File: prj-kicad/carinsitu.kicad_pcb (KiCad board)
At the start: 2 copper layers, 0 parts

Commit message: = ADD: Draw board outline, add fix holes
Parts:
- added FIX1: CONN_1, carinsitu:FIX, F.Cu at (100.8, 101.0)
- added FIX2: CONN_1, carinsitu:FIX, F.Cu at (100.8, 109.0)
- added FIX3: CONN_1, carinsitu:FIX, F.Cu at (175.2, 105.0)
- added FIX4: CONN_1, carinsitu:FIX, F.Cu at (190.8, 101.0)
- added FIX5: CONN_1, carinsitu:FIX, F.Cu at (190.8, 109.0)
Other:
- board outline added: 131.5 x 50 mm

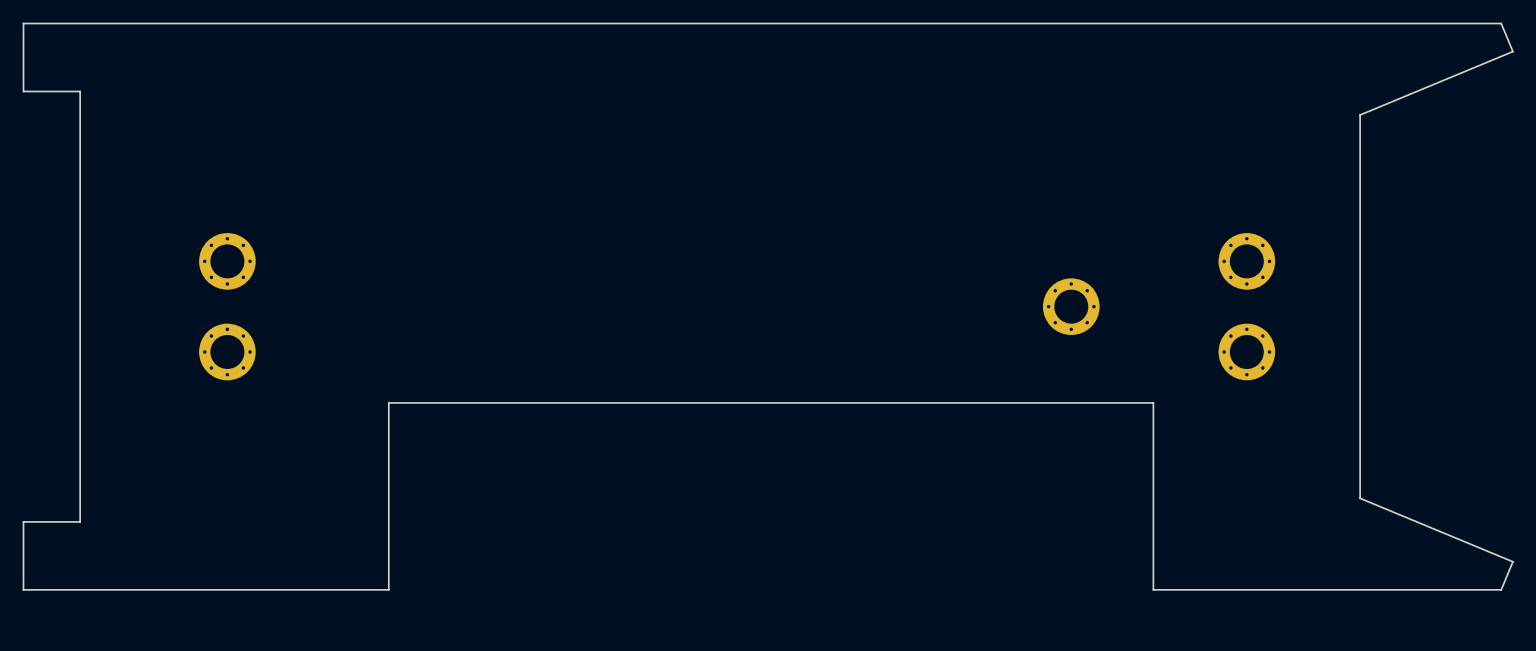
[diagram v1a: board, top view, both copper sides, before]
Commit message: = ADD: Place headlight LEDs, motor connector and ESC outline
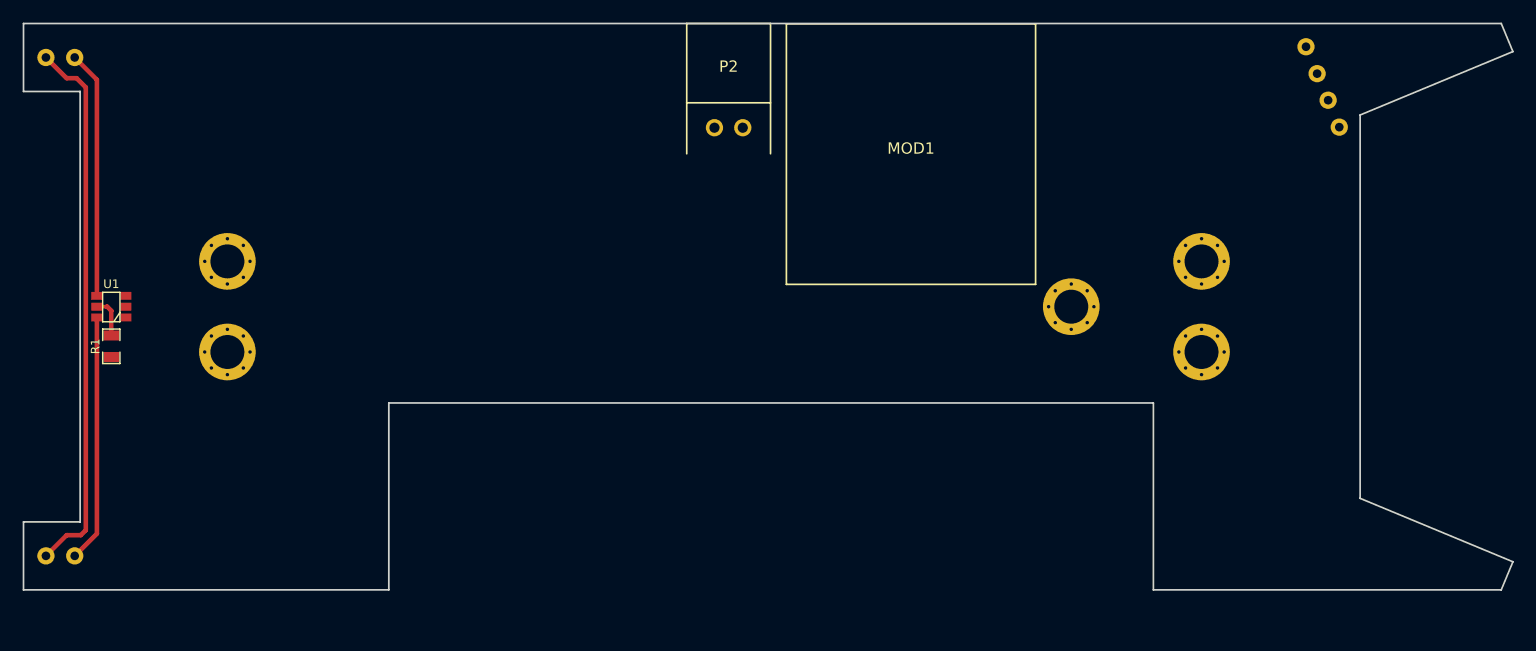
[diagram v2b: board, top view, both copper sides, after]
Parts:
- added D1: LED, carinsitu:LED, F.Cu at (86.0, 127.0)
- added D2: LED, carinsitu:LED, F.Cu at (86.0, 83.0)
- added MOD1: ESC, carinsitu:ESC, F.Cu at (161.1, 91.5)
- added P2: MOT, carinsitu:CONN_JST-XH-2, F.Cu at (145.0, 87.0)
- added R1: 10k, carinsitu:SMD0805, F.Cu at (90.5, 108.5)
- added REF**: LED-APA106, carinsitu:LED-APA106, F.Cu at (197.4, 85.6)
- added U1: MIC2860, carinsitu:SOT23-6, F.Cu at (90.5, 105.0)
- moved FIX4 4.00 mm to (186.8, 101.0)
- moved FIX5 4.00 mm to (186.8, 109.0)
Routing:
- net +5V: track 0.00 -> 48.2 mm
- net Net-(D2-Pad2): track 0.00 -> 21.9 mm
- net Net-(D1-Pad2): track 0.00 -> 21.9 mm
- net Net-(R1-Pad2): track 0.00 -> 3.61 mm
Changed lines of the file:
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@@
 (kicad_pcb (version 4) (host pcbnew 4.0.2+dfsg1-stable)
   (general
-    (links 44)
-    (no_connects 4)
+    (links 51)
+    (no_connects 7)
     (area 82.674999 79.924999 214.315001 130.075001)
     (thickness 1.6)
-    (drawings 23)
-    (tracks 0)
+    (drawings 25)
+    (tracks 15)
     (zones 0)
-    (modules 5)
-    (nets 2)
+    (modules 12)
+    (nets 9)
   )
   (page A4)
@@
   )
   (setup
-    (last_trace_width 0.25)
+    (last_trace_width 0.4064)
+    (user_trace_width 0.2032)
+    (user_trace_width 0.3048)
+    (user_trace_width 0.4064)
     (trace_clearance 0.2)
     (zone_clearance 0.508)
@@
   (net 0 "")
   (net 1 GND)
+  (net 2 "Net-(MOD1-Pad2)")
+  (net 3 "Net-(MOD1-Pad3)")
+  (net 4 +5V)
+  (net 5 "Net-(D1-Pad2)")
+  (net 6 "Net-(D2-Pad2)")
+  (net 7 "Net-(R1-Pad2)")
+  (net 8 HL_PWM)
   (net_class Default "This is the default net class."
     (clearance 0.2)
@@
     (uvia_dia 0.3)
     (uvia_drill 0.1)
+    (add_net +5V)
     (add_net GND)
+    (add_net HL_PWM)
+    (add_net "Net-(D1-Pad2)")
+    (add_net "Net-(D2-Pad2)")
+    (add_net "Net-(MOD1-Pad2)")
+    (add_net "Net-(MOD1-Pad3)")
+    (add_net "Net-(R1-Pad2)")
   )
   (module carinsitu:FIX locked (layer F.Cu)
@@
   )
   (module carinsitu:FIX locked (layer F.Cu)
-    (at 190.75 101)
+    (at 186.75 101)
     (fp_text reference FIX4 (at 0 0.8509) (layer F.SilkS) hide
       (effects (font (size 0.5 0.5) (thickness 0.125)))
@@
   )
   (module carinsitu:FIX locked (layer F.Cu)
-    (at 190.75 109)
+    (at 186.75 109)
     (fp_text reference FIX5 (at 0 0.8509) (layer F.SilkS) hide
       (effects (font (size 0.5 0.5) (thickness 0.125)))
@@
       (net 1 GND))
   )
+  (module carinsitu:CONN_JST-XH-2 (layer F.Cu)
+    (at 145 87 180)
+    (fp_text reference P2 (at 0 3.2 180) (layer F.SilkS)
+      (effects (font (size 1 1) (thickness 0.15)))
+    )
+    (fp_text value MOT (at 4.49 1.65 270) (layer F.Fab)
+      (effects (font (size 0.762 0.762) (thickness 0.15)))
+    )
+    (fp_line (start -3.7 0) (end 3.7 0) (layer F.SilkS) (width 0.15))
+    (fp_line (start 3.7 -4.5) (end 3.7 7) (layer F.SilkS) (width 0.15))
+    (fp_line (start 3.7 7) (end -3.7 7) (layer F.SilkS) (width 0.15))
+    (fp_line (start -3.7 7) (end -3.7 -4.5) (layer F.SilkS) (width 0.15))
+    (pad 1 thru_hole circle (at -1.25 -2.2 180) (size 1.524 1.524) (drill 0.9) (layers *.Cu *.Mask F.SilkS)
+      (net 2 "Net-(MOD1-Pad2)"))
+    (pad 2 thru_hole circle (at 1.25 -2.2 180) (size 1.524 1.524) (drill 0.9) (layers *.Cu *.Mask F.SilkS)
+      (net 3 "Net-(MOD1-Pad3)"))
+  )
+  (module carinsitu:LED-APA106 (layer F.Cu)
+    (at 197.44 85.6 292.5)
+    (autoplace_cost90 5)
+    (fp_text reference REF** (at 0 1.05 292.5) (layer F.SilkS) hide
+      (effects (font (size 0.5 0.5) (thickness 0.125)))
+    )
+    (fp_text value LED-APA106 (at 0 -1.2 292.5) (layer F.Fab)
+      (effects (font (size 0.762 0.762) (thickness 0.1016)))
+    )
+    (pad 1 thru_hole circle (at -3.84 0 292.5) (size 1.524 1.524) (drill 0.762) (layers *.Cu *.Mask F.SilkS))
+    (pad 2 thru_hole circle (at -1.27 0 292.5) (size 1.524 1.524) (drill 0.762) (layers *.Cu *.Mask F.SilkS))
+    (pad 3 thru_hole circle (at 1.27 0 292.5) (size 1.524 1.524) (drill 0.762) (layers *.Cu *.Mask F.SilkS))
+    (pad 4 thru_hole circle (at 3.84 0 292.5) (size 1.524 1.524) (drill 0.762) (layers *.Cu *.Mask F.SilkS))
+  )
+  (module carinsitu:LED locked (layer F.Cu)
+    (at 86 127)
+    (fp_text reference D1 (at 0 1.05) (layer F.SilkS) hide
+      (effects (font (size 0.5 0.5) (thickness 0.125)))
+    )
+    (fp_text value LED (at 0 -1.2) (layer F.Fab)
+      (effects (font (size 0.762 0.762) (thickness 0.1016)))
+    )
+    (pad 1 thru_hole circle (at -1.27 0) (size 1.524 1.524) (drill 0.762) (layers *.Cu *.Mask F.SilkS)
+      (net 4 +5V))
+    (pad 2 thru_hole circle (at 1.27 0) (size 1.524 1.524) (drill 0.762) (layers *.Cu *.Mask F.SilkS)
+      (net 5 "Net-(D1-Pad2)"))
+  )
+  (module carinsitu:LED locked (layer F.Cu)
+    (at 86 83)
+    (fp_text reference D2 (at 0 1.05) (layer F.SilkS) hide
+      (effects (font (size 0.5 0.5) (thickness 0.125)))
+    )
+    (fp_text value LED (at 0 -1.2) (layer F.Fab)
+      (effects (font (size 0.762 0.762) (thickness 0.1016)))
+    )
+    (pad 1 thru_hole circle (at -1.27 0) (size 1.524 1.524) (drill 0.762) (layers *.Cu *.Mask F.SilkS)
+      (net 4 +5V))
+    (pad 2 thru_hole circle (at 1.27 0) (size 1.524 1.524) (drill 0.762) (layers *.Cu *.Mask F.SilkS)
+      (net 6 "Net-(D2-Pad2)"))
+  )
+  (module carinsitu:SMD0805 (layer F.Cu)
+    (at 90.5 108.5 90)
+    (attr smd)
+    (fp_text reference R1 (at 0 -1.4 90) (layer F.SilkS)
+      (effects (font (size 0.762 0.762) (thickness 0.1016)))
+    )
+    (fp_text value 10k (at 0 0 90) (layer F.SilkS) hide
+      (effects (font (size 0.635 0.635) (thickness 0.127)))
+    )
+    (fp_line (start -0.508 0.762) (end -1.524 0.762) (layer F.SilkS) (width 0.127))
+    (fp_line (start -1.524 0.762) (end -1.524 -0.762) (layer F.SilkS) (width 0.127))
+    (fp_line (start -1.524 -0.762) (end -0.508 -0.762) (layer F.SilkS) (width 0.127))
+    (fp_line (start 0.508 -0.762) (end 1.524 -0.762) (layer F.SilkS) (width 0.127))
+    (fp_line (start 1.524 -0.762) (end 1.524 0.762) (layer F.SilkS) (width 0.127))
+    (fp_line (start 1.524 0.762) (end 0.508 0.762) (layer F.SilkS) (width 0.127))
+    (pad 1 smd rect (at -0.9525 0 90) (size 0.889 1.397) (layers F.Cu F.Paste F.Mask)
+      (net 1 GND))
+    (pad 2 smd rect (at 0.9525 0 90) (size 0.889 1.397) (layers F.Cu F.Paste F.Mask)
+      (net 7 "Net-(R1-Pad2)"))
+    (model smd/chip_cms.wrl
+      (at (xyz 0 0 0))
+      (scale (xyz 0.1 0.1 0.1))
+      (rotate (xyz 0 0 0))
+    )
+  )
+  (module carinsitu:SOT23-6 (layer F.Cu)
+    (at 90.5 105 90)
+    (fp_text reference U1 (at 1.99898 0 180) (layer F.SilkS)
+      (effects (font (size 0.762 0.762) (thickness 0.0762)))
+    )
+    (fp_text value MIC2860 (at 0.0635 0 90) (layer F.SilkS) hide
+      (effects (font (size 0.50038 0.50038) (thickness 0.0762)))
+    )
+    (fp_line (start -0.508 0.762) (end -1.27 0.254) (layer F.SilkS) (width 0.127))
+    (fp_line (start 1.27 0.762) (end -1.3335 0.762) (layer F.SilkS) (width 0.127))
+    (fp_line (start -1.3335 0.762) (end -1.3335 -0.762) (layer F.SilkS) (width 0.127))
+    (fp_line (start -1.3335 -0.762) (end 1.27 -0.762) (layer F.SilkS) (width 0.127))
+    (fp_line (start 1.27 -0.762) (end 1.27 0.762) (layer F.SilkS) (width 0.127))
+    (pad 6 smd rect (at -0.9525 -1.27 90) (size 0.70104 1.00076) (layers F.Cu F.Paste F.Mask)
+      (net 5 "Net-(D1-Pad2)"))
+    (pad 5 smd rect (at 0 -1.27 90) (size 0.70104 1.00076) (layers F.Cu F.Paste F.Mask)
+      (net 7 "Net-(R1-Pad2)"))
+    (pad 4 smd rect (at 0.9525 -1.27 90) (size 0.70104 1.00076) (layers F.Cu F.Paste F.Mask)
+      (net 6 "Net-(D2-Pad2)"))
+    (pad 3 smd rect (at 0.9525 1.27 90) (size 0.70104 1.00076) (layers F.Cu F.Paste F.Mask)
+      (net 4 +5V))
+    (pad 2 smd rect (at 0 1.27 90) (size 0.70104 1.00076) (layers F.Cu F.Paste F.Mask)
+      (net 1 GND))
+    (pad 1 smd rect (at -0.9525 1.27 90) (size 0.70104 1.00076) (layers F.Cu F.Paste F.Mask)
+      (net 8 HL_PWM))
+    (model smd/SOT23_6.wrl
+      (at (xyz 0 0 0))
+      (scale (xyz 0.11 0.11 0.11))
+      (rotate (xyz 0 0 -180))
+    )
+  )
+  (module carinsitu:ESC (layer F.Cu)
+    (at 161.1 91.53 180)
+    (fp_text reference MOD1 (at 0 0.5 180) (layer F.SilkS)
+      (effects (font (size 1 1) (thickness 0.15)))
+    )
+    (fp_text value ESC (at 0 -0.5 180) (layer F.Fab)
+      (effects (font (size 1 1) (thickness 0.15)))
+    )
+    (fp_line (start -11 -11.5) (end 11 -11.5) (layer F.SilkS) (width 0.15))
+    (fp_line (start 11 -11.5) (end 11 11.5) (layer F.SilkS) (width 0.15))
+    (fp_line (start 11 11.5) (end -11 11.5) (layer F.SilkS) (width 0.15))
+    (fp_line (start -11 11.5) (end -11 -11.5) (layer F.SilkS) (width 0.15))
+  )
+  (gr_line (start 210.93 80) (end 197.44 85.6) (angle 90) (layer Dwgs.User) (width 0.1))
+  (gr_line (start 210.93 80) (end 210.93 79) (angle 90) (layer Dwgs.User) (width 0.1))
   (gr_line (start 199.25 113.5) (end 182.5 113.5) (angle 90) (layer Dwgs.User) (width 0.15))
   (gr_line (start 96 113.5) (end 96 96.5) (angle 90) (layer Dwgs.User) (width 0.15))
@@
   (gr_line (start 213.21 80) (end 214.24 82.48) (angle 90) (layer Edge.Cuts) (width 0.15))
   (gr_line (start 82.75 80) (end 213.21 80) (angle 90) (layer Edge.Cuts) (width 0.15))
+  (segment (start 86.56 84.83) (end 87.44 84.83) (width 0.4064) (layer F.Cu) (net 4))
+  (segment (start 87.81 125.17) (end 88.25 124.73) (width 0.4064) (layer F.Cu) (net 4))
+  (segment (start 88.25 124.73) (end 88.25 85.64) (width 0.4064) (layer F.Cu) (net 4))
+  (segment (start 84.73 127) (end 86.56 125.17) (width 0.4064) (layer F.Cu) (net 4) (status 400000))
+  (segment (start 86.56 125.17) (end 87.81 125.17) (width 0.4064) (layer F.Cu) (net 4))
+  (segment (start 86.56 84.83) (end 84.73 83) (width 0.4064) (layer F.Cu) (net 4) (status 800000))
+  (segment (start 87.44 84.83) (end 88.25 85.64) (width 0.4064) (layer F.Cu) (net 4))
+  (segment (start 89.23 105.9525) (end 89.23 125.04) (width 0.4064) (layer F.Cu) (net 5))
+  (segment (start 89.23 125.04) (end 87.27 127) (width 0.4064) (layer F.Cu) (net 5))
+  (segment (start 89.23 104.0475) (end 89.23 84.96) (width 0.4064) (layer F.Cu) (net 6))
+  (segment (start 89.23 84.96) (end 87.27 83) (width 0.4064) (layer F.Cu) (net 6))
+  (segment (start 89.23 105) (end 90.05 105) (width 0.3048) (layer F.Cu) (net 7))
+  (segment (start 90.5 105.36) (end 90.14 105) (width 0.4064) (layer F.Cu) (net 7))
+  (segment (start 90.14 105) (end 90.05 105) (width 0.4064) (layer F.Cu) (net 7))
+  (segment (start 90.5 105.36) (end 90.5 107.5475) (width 0.4064) (layer F.Cu) (net 7))
 )

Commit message: = ADD: Create ESP32 interface ; create schematics and footprint for Wemos D1-Mini (not fully routed)
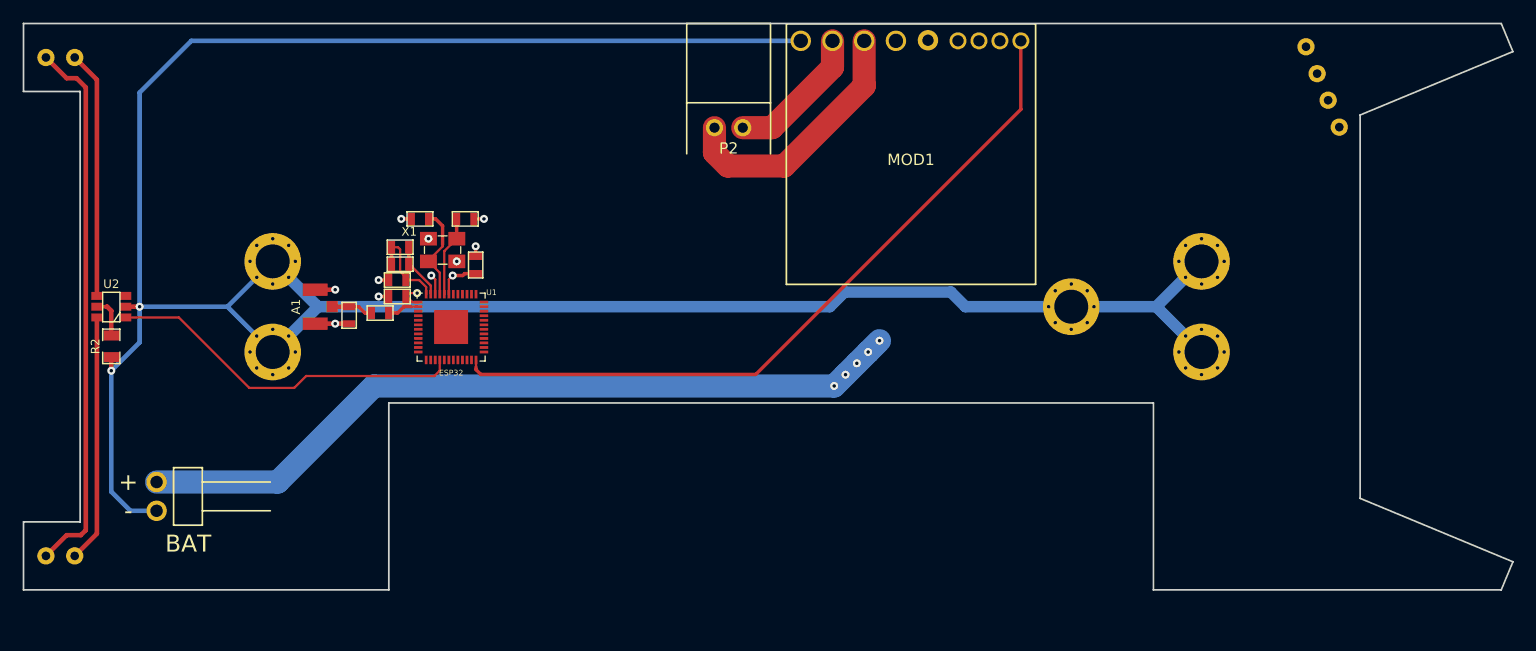
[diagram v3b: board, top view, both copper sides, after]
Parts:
- added A1: ANTENNA, carinsitu:CONN_UFL-R-SMT-1, F.Cu at (108.5, 105.0)
- added C1: 10nF, carinsitu:SMD0603, F.Cu at (115.8, 102.7)
- added C10: C, carinsitu:SMD0603, F.Cu at (115.8, 104.1)
- added C11: C, carinsitu:SMD0603, F.Cu at (122.7, 101.3)
- added C2: 3.3nF, carinsitu:SMD0603, F.Cu at (116.0, 101.2)
- added C3: C, carinsitu:SMD0603, F.Cu at (111.5, 105.8)
- added C4: C, carinsitu:SMD0603, F.Cu at (117.8, 97.2)
- added C5: C, carinsitu:SMD0603, F.Cu at (121.8, 97.2)
- added L1: INDUCTOR, carinsitu:SMD0603, F.Cu at (114.2, 105.6)
- added P1: BAT, carinsitu:CONN_61300211021, F.Cu at (94.5, 121.8)
- added R1: 20k, carinsitu:SMD0603, F.Cu at (116.0, 99.8)
- added U1: ESP32, carinsitu:QFN48-04, F.Cu at (120.5, 106.8)
- added X1: 40MHz, carinsitu:Q_3.2x2.5, F.Cu at (119.8, 100.0)
- moved FIX1 4.00 mm to (104.8, 101.0)
- moved FIX2 4.00 mm to (104.8, 109.0)
- turned MOD1 to 0 degrees
- renumbered R1 to R2, U1 to U2
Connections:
- P2 pad 1: Net-(MOD1-Pad2) -> GND
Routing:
- net GND: track 0.00 -> 276.5 mm, vias 0 -> 11
- net Net-(MOD1-Pad4): track 0.00 -> 101.7 mm, vias 0 -> 5
- net PPM_ESC: track 0.00 -> 64.9 mm
- net HL_PWM: track 0.00 -> 31.9 mm
- net Net-(MOD1-Pad3): track 0.00 -> 22.8 mm
- net +3V3: track 0.00 -> 12.1 mm, vias 0 -> 3
- net Net-(C4-Pad1): track 0.00 -> 8.46 mm
- net Net-(C1-Pad1): track 0.00 -> 7.94 mm
- net Net-(C5-Pad1): track 0.00 -> 7.11 mm
- net Net-(C2-Pad1): track 0.00 -> 4.99 mm
- net Net-(A1-Pad1): track 0.00 -> 3.70 mm
- net Net-(L1-Pad1): track 0.00 -> 2.84 mm
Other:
- copper layers 2 -> 4
- net class Default: clearance 0.2 -> 0.1524; trace_width 0.25 -> 0.2032
- rule trace_clearance: 0.2 -> 0.1524
- board text added: "+"
- board text added: "-"
